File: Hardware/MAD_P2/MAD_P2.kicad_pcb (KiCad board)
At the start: 4 copper layers, 121.6 x 145.5 mm, 363 parts, among them J1 Line_1_3, J10 Conn_02x05_Odd_Even, J11 Conn_02x05_Odd_Even, J12 Line_3_3, J13 Conn_02x05_Odd_Even, J14 Conn_02x05_Odd_Even, J15 Conn_ADC1, J16 Conn_DAC, J17 Line_1_2, J18 P3, J19 P4, J2 Line_2_2, J20 P2, J21 Conn_02x05_Odd_Even, J22 Conn_02x05_Odd_Even, J23 Conn_02x03_Odd_Even, J24 P5, J25 P6, J26 P7, J27 Line_1_1, J28 Line_2_1, J29 Line_2_3, J3 Line_3_1, J30 Line_3_2, J31 Micro_SD_Card_Connector, J32 Micro_SD_Card_Socket, J33 Shifted IO, J4 Power_In, J5 Micro_SD_Card, J6 Edge_Conn, J7 Conn_02x05_Odd_Even, J8 USB_C_Receptacle_USB2.0, J9 Conn_02x05_Odd_Even, P10 CONN_01X01, P11 CONN_01X01, P13 CONN_01X01, P8 CONN_01X01, Q1 MMBT3904, Q2 2N7002, Q3 2N7002, Q4 2N7002, Q5 2N7002, SW1 Switch_SW_Push, U1 P2X8C4M64P-REF, U10 AMS1117-3.3, U11 APM4953, U12 APM4953, U13 XL1509-5.0, U14 XL1509-5.0, U15 AMS1117-3.3, U16 AMS1117-3.3, U17 MAX5134-7, U18 AMS1117-3.3, U19 AMS1117-1.8, U2 XL1509-5.0, U20 LM321, U21 APM4953, U22 XL1509-5.0, U23 ADS131A04, U24 AMS1117-3.3, U26 W25Q128JVS, U27 FT232RL, U28 DS3231M, U29 ESP-12F, U3 XL1509-5.0, U4 XL1509-5.0, U5 XL1509-5.0, U6 AMS1117-3.3, U7 AMS1117-3.3, U8 AMS1117-3.3, U9 AMS1117-3.3, Y1 20MHz, Y2 16.384MHz

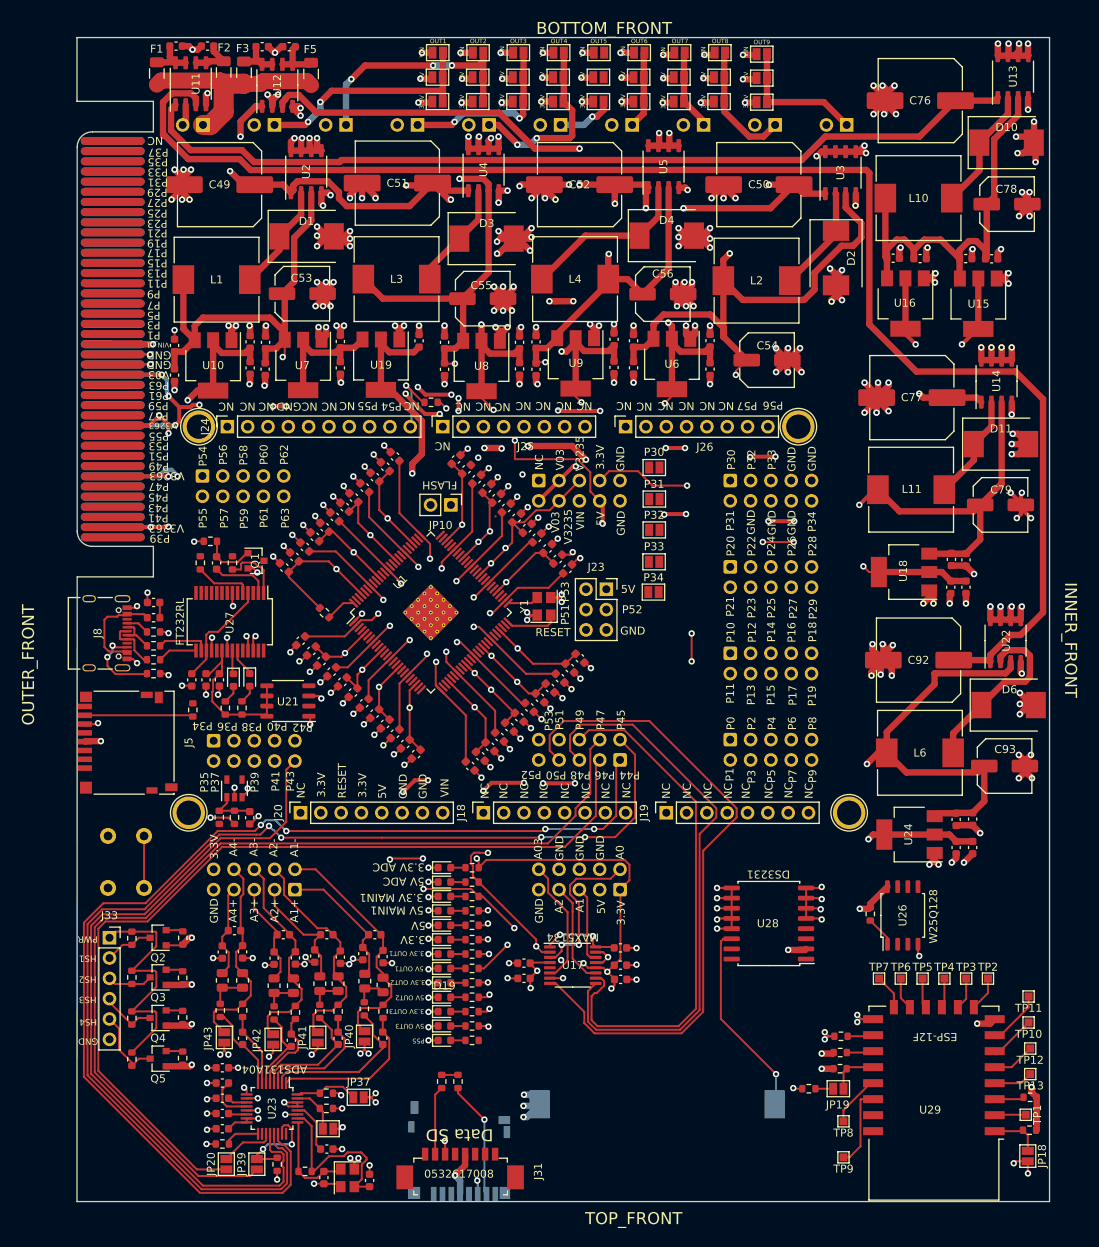
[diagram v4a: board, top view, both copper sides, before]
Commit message: errors with connections to edge module fixed, created new dsn for autorouting
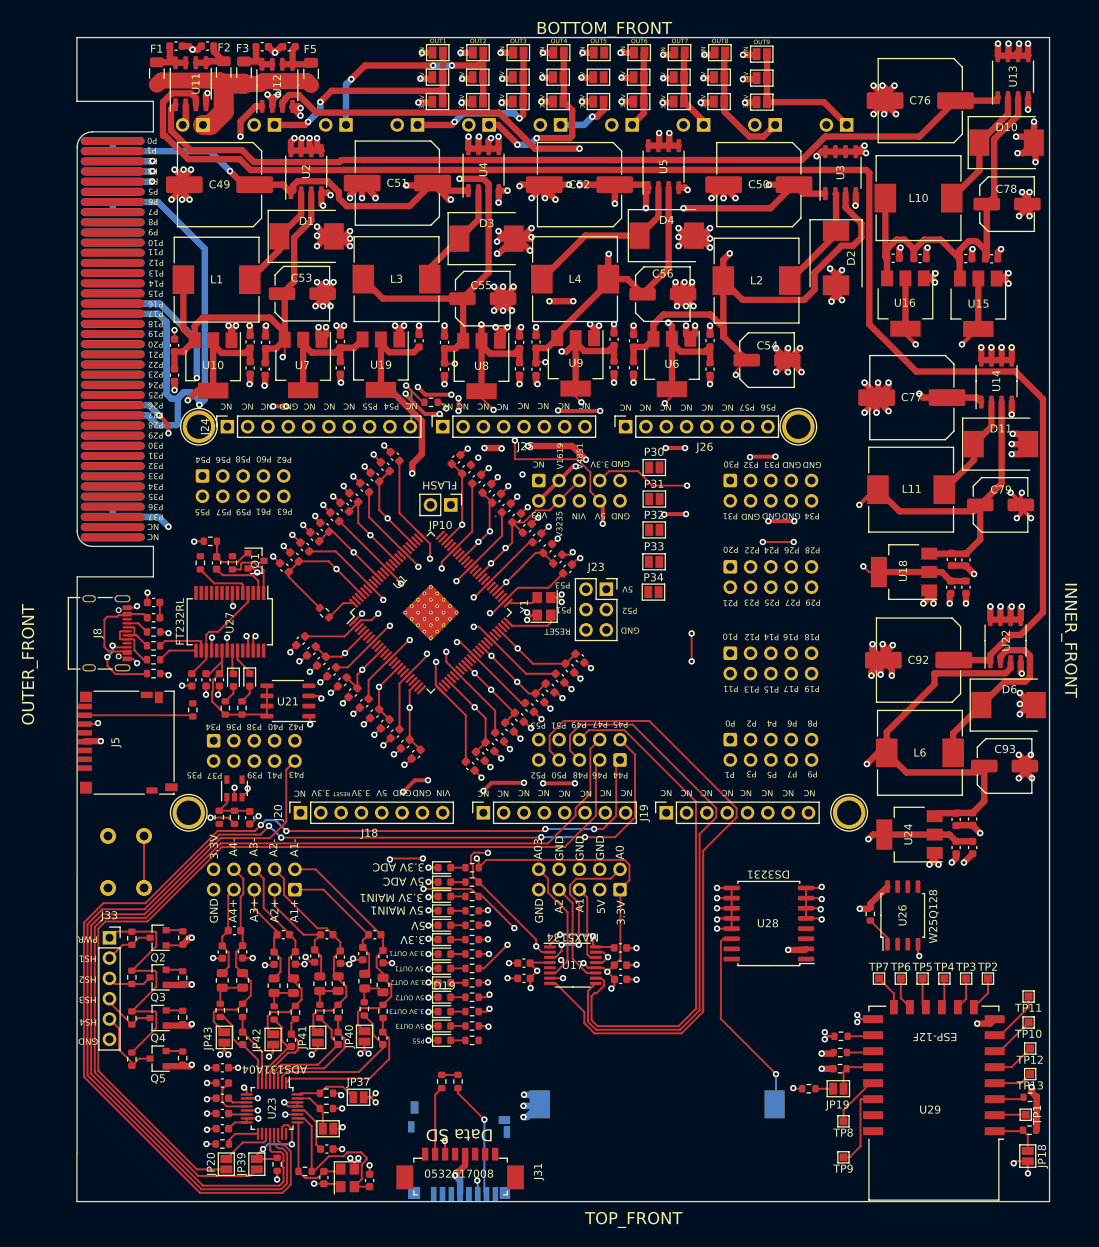
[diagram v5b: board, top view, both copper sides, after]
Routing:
- net V_0_3: track 312.1 -> 336.2 mm, vias 30 -> 26
- net V_32_35: track 315.3 -> 322.5 mm, vias 18 -> 17
- net VIN_L1: track 284.8 -> 291.7 mm, vias 15 -> 14
- net GND: track 619.0 -> 624.6 mm, vias 342 -> 344
- net P22: track 4.75 -> 0.05 mm, vias 1 -> 0
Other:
- board text added: "RST"
- board text removed: "V3263"
- board text removed: "VIN_L1"

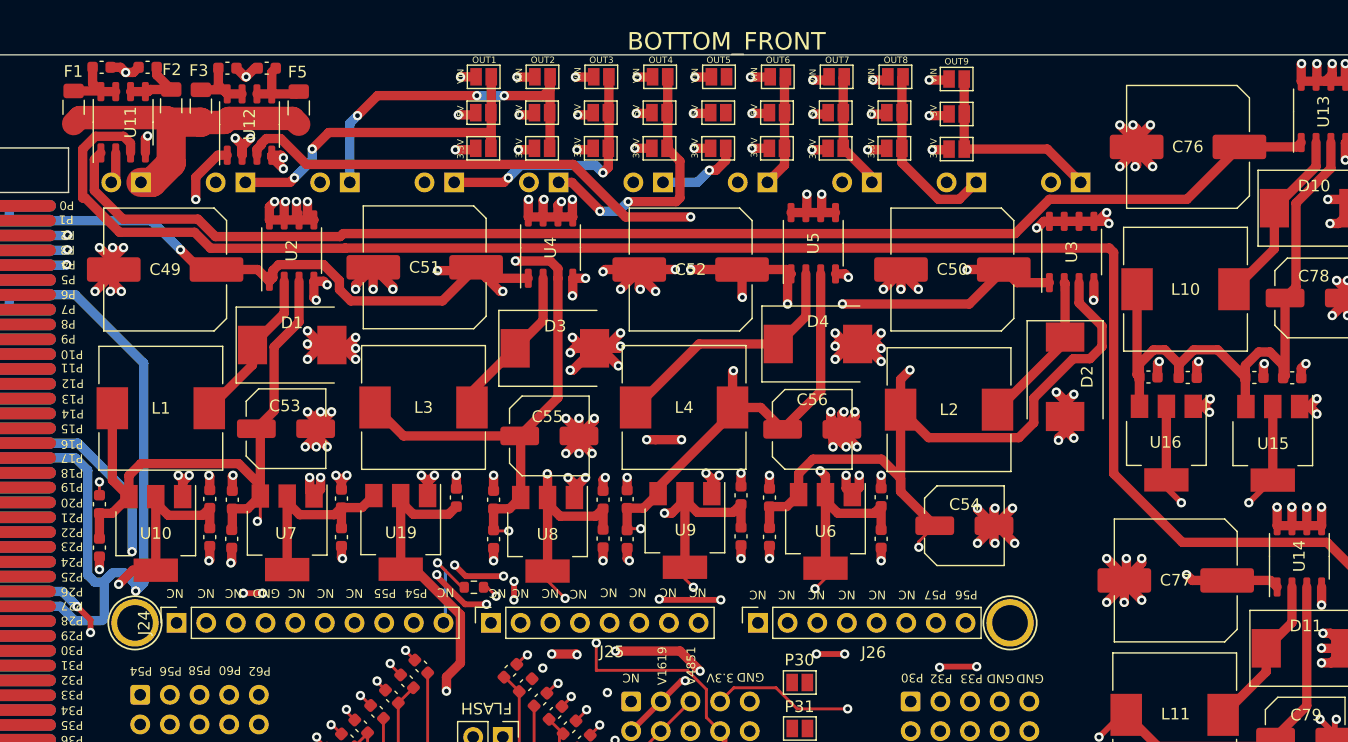
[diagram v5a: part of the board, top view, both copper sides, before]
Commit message: re-routed power lines to edge module for optimized routes
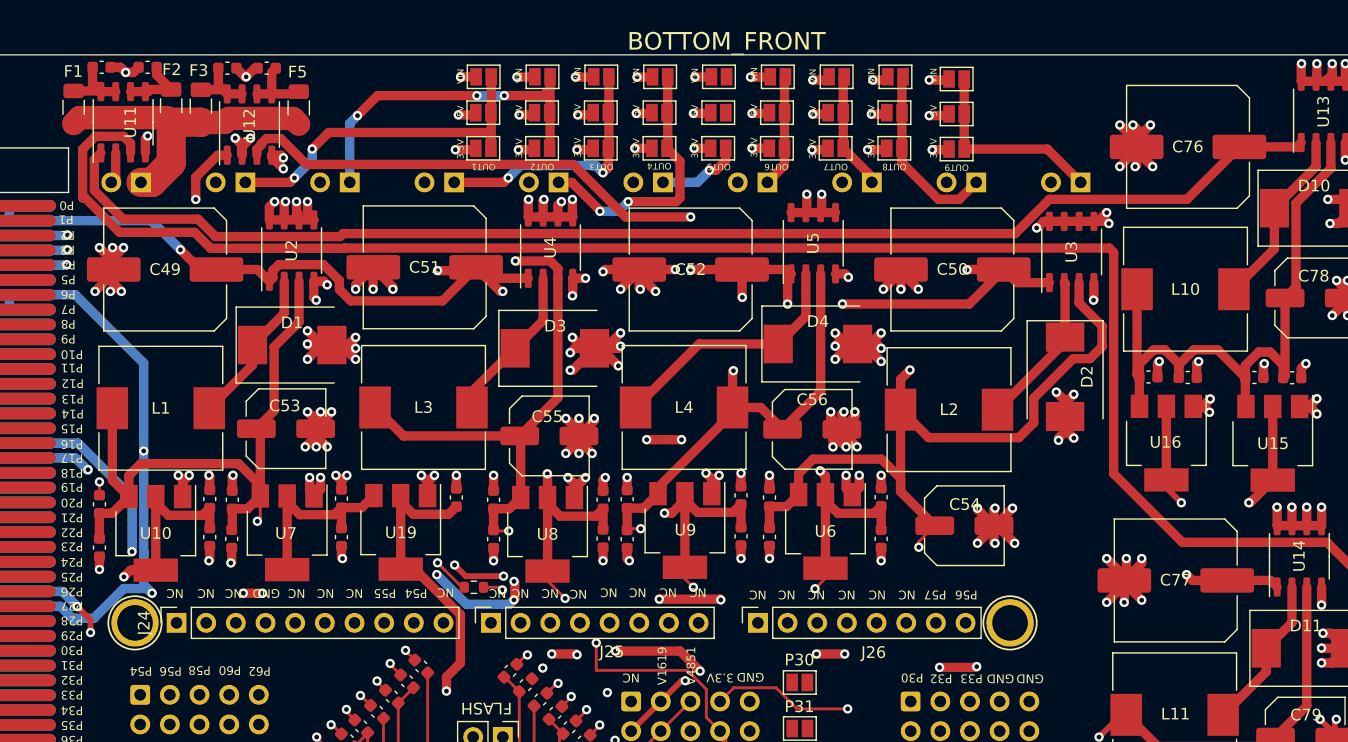
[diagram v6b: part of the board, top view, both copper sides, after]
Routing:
- net VIN_L1: track 291.7 -> 266.1 mm
- net V_0_3: track 336.2 -> 327.3 mm, vias 26 -> 27
- net Net-(J24-Pad10): track 8.64 -> 4.31 mm

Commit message: backup push before dsn import
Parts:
- moved C17 39.1 mm to (440.1, 106.0), turned to 315 degrees
- moved C41 38.9 mm to (433.0, 68.5), turned to 135 degrees
- moved C44 37.7 mm to (419.3, 82.0), turned to 135 degrees
- moved C20 37.4 mm to (439.2, 67.8), turned to 45 degrees
- moved C22 37.4 mm to (435.6, 105.3), turned to 225 degrees
- moved C25 37.2 mm to (431.7, 69.7), turned to 135 degrees
- moved C27 37.2 mm to (441.3, 104.7), turned to 315 degrees
- moved C46 37.1 mm to (453.9, 92.1), turned to 315 degrees
- moved C43 36.1 mm to (420.5, 80.7), turned to 135 degrees
- moved C26 35.8 mm to (430.5, 70.9), turned to 135 degrees
- moved C28 35.5 mm to (442.6, 103.4), turned to 315 degrees
- moved C45 35.5 mm to (452.6, 93.4), turned to 315 degrees
- moved C21 35.4 mm to (434.3, 104.1), turned to 225 degrees
- moved C19 35.4 mm to (440.6, 69.0), turned to 45 degrees
- moved C30 34.9 mm to (421.8, 79.5), turned to 135 degrees
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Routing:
- net +5V_1: track 178.5 -> 77.4 mm, vias 6 -> 4
- net +5V_2: track 169.7 -> 77.8 mm, vias 6 -> 4
- net +3.3V_2: track 146.9 -> 65.4 mm, vias 6 -> 4
- net +3.3V_1: track 135.8 -> 62.2 mm, vias 6 -> 4
- net VIN_L1: track 266.1 -> 245.5 mm, vias 14 -> 10
- net V_32_35: track 322.5 -> 305.1 mm, vias 17 -> 16
- net +1V8: track 225.1 -> 216.1 mm
- net GND: track 624.6 -> 629.5 mm
- net V_0_3: track 327.3 -> 330.3 mm, vias 27 -> 25
- net Net-(U1-Pad51): track 3.92 -> 3.02 mm
- net RESET: track 10.3 -> 9.41 mm
